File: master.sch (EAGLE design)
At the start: 24 parts, among them IC1 MEGA164P/324P/644P-PU, SW1 CI-11, U2 3V3 something

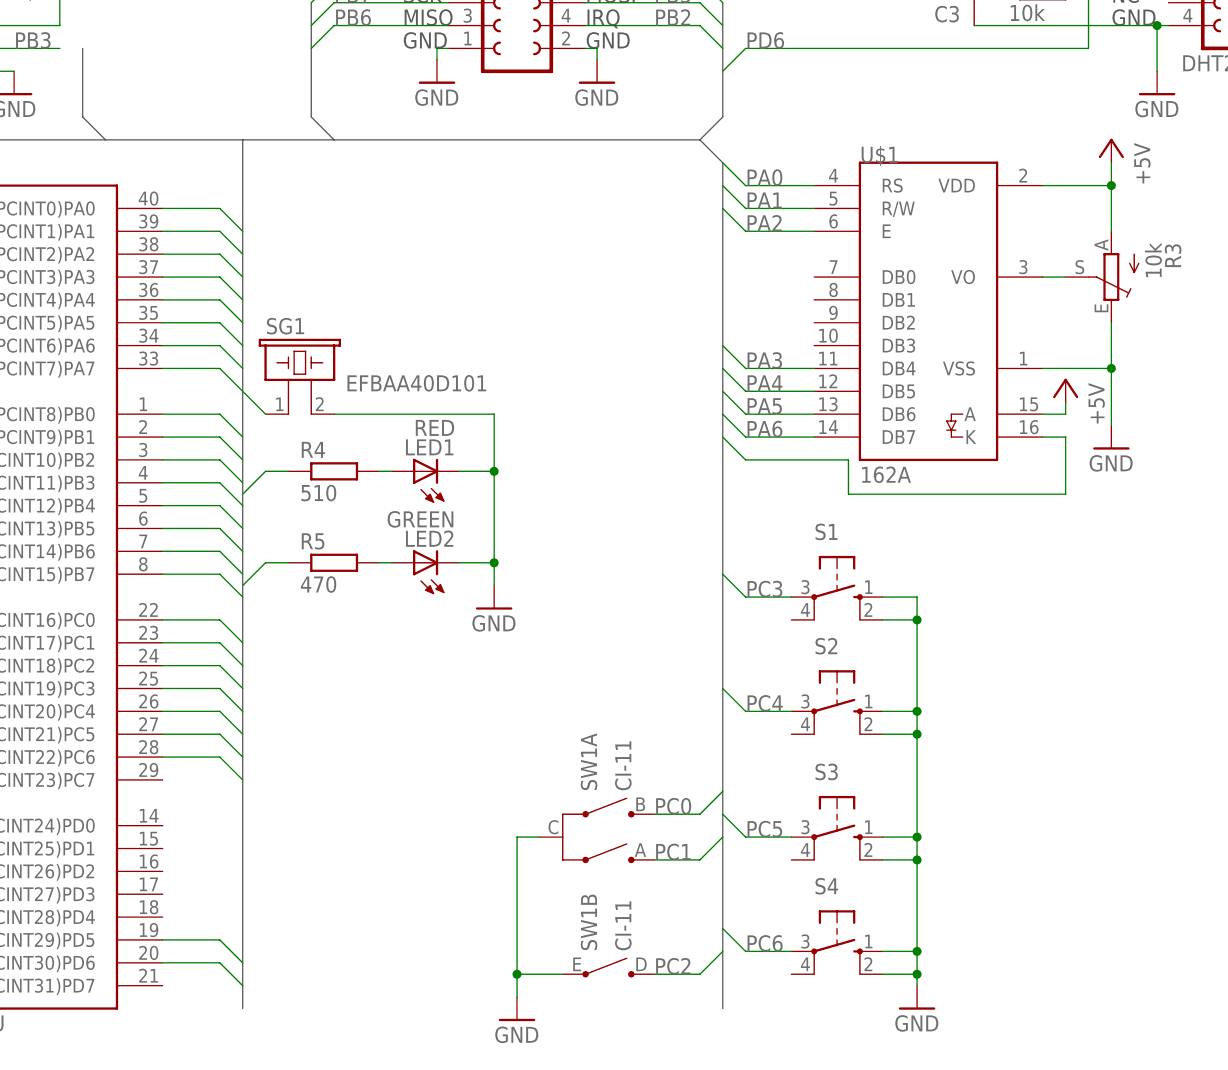
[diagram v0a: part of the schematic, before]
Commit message: added watch crystal to master, notes for sensor
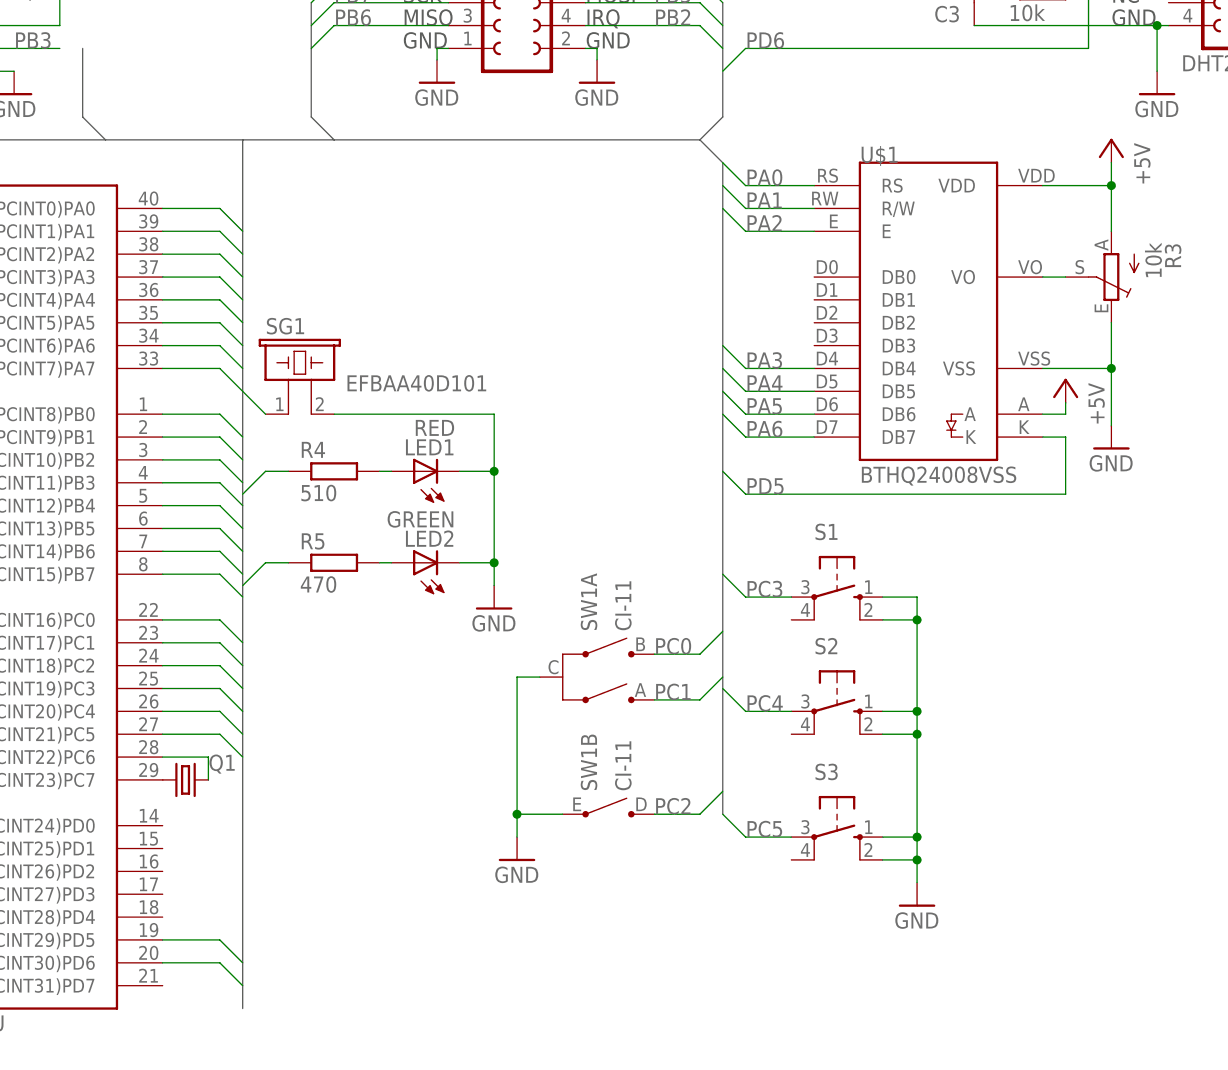
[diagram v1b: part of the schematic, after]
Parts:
- removed S4: (no value), switch-omron:10-XX
- added Q1: (no value), crystal:CRYSTALTC26H
- U$1: value 162A -> BTHQ24008VSS; device lcd_displays:162A -> lcd_displays:BTHQ24008VSS
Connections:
- removed net PC6: IC1.(TOSC1/PCINT22)PC6, S4.P
- new net N$3: IC1.(TOSC2/PCINT23)PC7, Q1.1
- new net N$4: IC1.(TOSC1/PCINT22)PC6, Q1.2
- net GND: no longer S4.S, S4.S1
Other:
- moved on the sheet: SW1A, SW1B

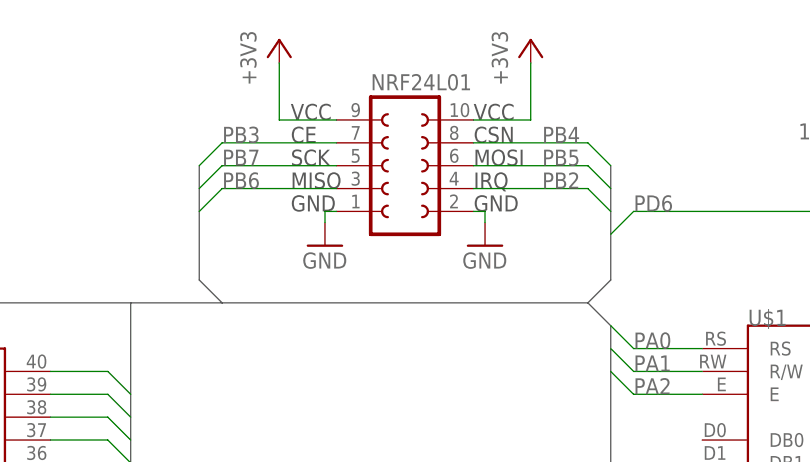
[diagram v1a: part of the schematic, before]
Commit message: series resistors for shared spi/isp interface
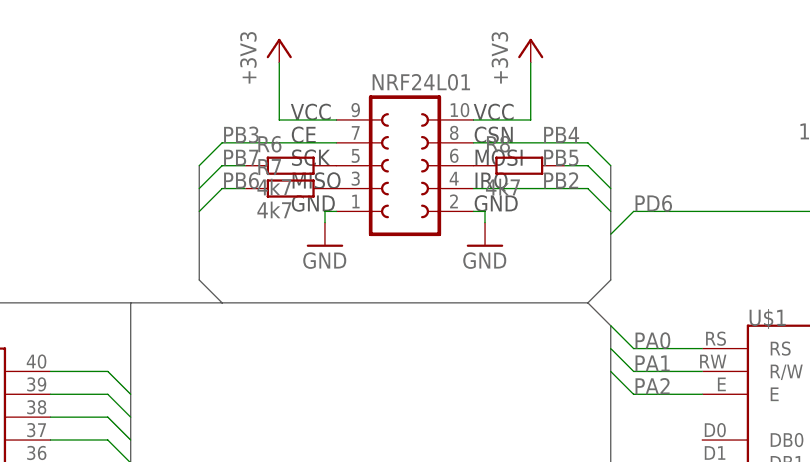
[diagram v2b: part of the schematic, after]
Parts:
- added R6, R7, R8: 4k7, rcl:R-EU_0207/7
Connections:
- new net N$5: NRF24L01.5, R6.2
- new net N$6: NRF24L01.3, R7.2
- new net N$7: NRF24L01.6, R8.1
- net PB5: now also R8.2; no longer NRF24L01.6
- net PB6: now also R7.1; no longer NRF24L01.3
- net PB7: now also R6.1; no longer NRF24L01.5
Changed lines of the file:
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@@
 <setting verticaltext="up"/>
 </settings>
-<grid distance="1.27" unitdist="mm" unit="mm" style="lines" multiple="1" display="yes" altdistance="635" altunitdist="mic" altunit="mic"/>
+<grid distance="0.1" unitdist="inch" unit="mm" style="lines" multiple="1" display="yes" altdistance="0.01" altunitdist="inch" altunit="mm"/>
 <layers>
-<layer number="1" name="Top" color="4" fill="1" visible="yes" active="no"/>
-<layer number="2" name="Route2" color="1" fill="3" visible="yes" active="no"/>
-<layer number="3" name="Route3" color="4" fill="3" visible="yes" active="no"/>
-<layer number="4" name="Route4" color="1" fill="4" visible="yes" active="no"/>
-<layer number="5" name="Route5" color="4" fill="4" visible="yes" active="no"/>
-<layer number="6" name="Route6" color="1" fill="8" visible="yes" active="no"/>
-<layer number="7" name="Route7" color="4" fill="8" visible="yes" active="no"/>
-<layer number="8" name="Route8" color="1" fill="2" visible="yes" active="no"/>
-<layer number="9" name="Route9" color="4" fill="2" visible="yes" active="no"/>
-<layer number="10" name="Route10" color="1" fill="7" visible="yes" active="no"/>
-<layer number="11" name="Route11" color="4" fill="7" visible="yes" active="no"/>
-<layer number="12" name="Route12" color="1" fill="5" visible="yes" active="no"/>
-<layer number="13" name="Route13" color="4" fill="5" visible="yes" active="no"/>
-<layer number="14" name="Route14" color="1" fill="6" visible="yes" active="no"/>
-<layer number="15" name="Route15" color="4" fill="6" visible="yes" active="no"/>
-<layer number="16" name="Bottom" color="1" fill="1" visible="yes" active="no"/>
-<layer number="17" name="Pads" color="2" fill="1" visible="yes" active="no"/>
-<layer number="18" name="Vias" color="2" fill="1" visible="yes" active="no"/>
-<layer number="19" name="Unrouted" color="6" fill="1" visible="yes" active="no"/>
-<layer number="20" name="Dimension" color="15" fill="1" visible="yes" active="no"/>
-<layer number="21" name="tPlace" color="7" fill="1" visible="yes" active="no"/>
-<layer number="22" name="bPlace" color="7" fill="1" visible="yes" active="no"/>
-<layer number="23" name="tOrigins" color="15" fill="1" visible="yes" active="no"/>
-<layer number="24" name="bOrigins" color="15" fill="1" visible="yes" active="no"/>
-<layer number="25" name="tNames" color="7" fill="1" visible="yes" active="no"/>
-<layer number="26" name="bNames" color="7" fill="1" visible="yes" active="no"/>
-<layer number="27" name="tValues" color="7" fill="1" visible="yes" active="no"/>
-<layer number="28" name="bValues" color="7" fill="1" visible="yes" active="no"/>
+<layer number="1" name="Top" color="4" fill="1" visible="no" active="no"/>
+<layer number="2" name="Route2" color="1" fill="3" visible="no" active="no"/>
+<layer number="3" name="Route3" color="4" fill="3" visible="no" active="no"/>
+<layer number="4" name="Route4" color="1" fill="4" visible="no" active="no"/>
+<layer number="5" name="Route5" color="4" fill="4" visible="no" active="no"/>
+<layer number="6" name="Route6" color="1" fill="8" visible="no" active="no"/>
+<layer number="7" name="Route7" color="4" fill="8" visible="no" active="no"/>
+<layer number="8" name="Route8" color="1" fill="2" visible="no" active="no"/>
+<layer number="9" name="Route9" color="4" fill="2" visible="no" active="no"/>
+<layer number="10" name="Route10" color="1" fill="7" visible="no" active="no"/>
+<layer number="11" name="Route11" color="4" fill="7" visible="no" active="no"/>
+<layer number="12" name="Route12" color="1" fill="5" visible="no" active="no"/>
+<layer number="13" name="Route13" color="4" fill="5" visible="no" active="no"/>
+<layer number="14" name="Route14" color="1" fill="6" visible="no" active="no"/>
+<layer number="15" name="Route15" color="4" fill="6" visible="no" active="no"/>
+<layer number="16" name="Bottom" color="1" fill="1" visible="no" active="no"/>
+<layer number="17" name="Pads" color="2" fill="1" visible="no" active="no"/>
+<layer number="18" name="Vias" color="2" fill="1" visible="no" active="no"/>
+<layer number="19" name="Unrouted" color="6" fill="1" visible="no" active="no"/>
+<layer number="20" name="Dimension" color="15" fill="1" visible="no" active="no"/>
+<layer number="21" name="tPlace" color="7" fill="1" visible="no" active="no"/>
+<layer number="22" name="bPlace" color="7" fill="1" visible="no" active="no"/>
+<layer number="23" name="tOrigins" color="15" fill="1" visible="no" active="no"/>
+<layer number="24" name="bOrigins" color="15" fill="1" visible="no" active="no"/>
+<layer number="25" name="tNames" color="7" fill="1" visible="no" active="no"/>
+<layer number="26" name="bNames" color="7" fill="1" visible="no" active="no"/>
+<layer number="27" name="tValues" color="7" fill="1" visible="no" active="no"/>
+<layer number="28" name="bValues" color="7" fill="1" visible="no" active="no"/>
 <layer number="29" name="tStop" color="7" fill="3" visible="no" active="no"/>
 <layer number="30" name="bStop" color="7" fill="6" visible="no" active="no"/>
@@
 <layer number="35" name="tGlue" color="7" fill="4" visible="no" active="no"/>
 <layer number="36" name="bGlue" color="7" fill="5" visible="no" active="no"/>
-<layer number="37" name="tTest" color="7" fill="1" visible="yes" active="no"/>
-<layer number="38" name="bTest" color="7" fill="1" visible="yes" active="no"/>
+<layer number="37" name="tTest" color="7" fill="1" visible="no" active="no"/>
+<layer number="38" name="bTest" color="7" fill="1" visible="no" active="no"/>
 <layer number="39" name="tKeepout" color="4" fill="11" visible="no" active="no"/>
 <layer number="40" name="bKeepout" color="1" fill="11" visible="no" active="no"/>
@@
 <layer number="44" name="Drills" color="7" fill="1" visible="no" active="no"/>
 <layer number="45" name="Holes" color="7" fill="1" visible="no" active="no"/>
-<layer number="46" name="Milling" color="3" fill="1" visible="yes" active="no"/>
-<layer number="47" name="Measures" color="7" fill="1" visible="yes" active="no"/>
-<layer number="48" name="Document" color="7" fill="1" visible="yes" active="no"/>
-<layer number="49" name="Reference" color="7" fill="1" visible="yes" active="no"/>
-<layer number="50" name="dxf" color="7" fill="1" visible="yes" active="no"/>
-<layer number="51" name="tDocu" color="7" fill="1" visible="yes" active="no"/>
-<layer number="52" name="bDocu" color="7" fill="1" visible="yes" active="no"/>
-<layer number="53" name="tPadExt" color="7" fill="1" visible="yes" active="no"/>
-<layer number="54" name="bPadExt" color="1" fill="1" visible="yes" active="no"/>
+<layer number="46" name="Milling" color="3" fill="1" visible="no" active="no"/>
+<layer number="47" name="Measures" color="7" fill="1" visible="no" active="no"/>
+<layer number="48" name="Document" color="7" fill="1" visible="no" active="no"/>
+<layer number="49" name="Reference" color="7" fill="1" visible="no" active="no"/>
+<layer number="50" name="dxf" color="7" fill="1" visible="no" active="no"/>
+<layer number="51" name="tDocu" color="7" fill="1" visible="no" active="no"/>
+<layer number="52" name="bDocu" color="7" fill="1" visible="no" active="no"/>
+<layer number="53" name="tPadExt" color="7" fill="1" visible="no" active="no"/>
+<layer number="54" name="bPadExt" color="1" fill="1" visible="no" active="no"/>
 <layer number="91" name="Nets" color="2" fill="1" visible="yes" active="yes"/>
 <layer number="92" name="Busses" color="1" fill="1" visible="yes" active="yes"/>
@@
 <part name="+3V3" library="supply1" deviceset="+3V3" device=""/>
 <part name="Q1" library="crystal" deviceset="CRYSTAL" device="TC26H"/>
+<part name="R6" library="rcl" deviceset="R-EU_" device="0207/7" value="4k7"/>
+<part name="R7" library="rcl" deviceset="R-EU_" device="0207/7" value="4k7"/>
+<part name="R8" library="rcl" deviceset="R-EU_" device="0207/7" value="4k7"/>
 </parts>
 <sheets>
@@
 <instance part="+3V3" gate="G$1" x="166.37" y="166.37"/>
 <instance part="Q1" gate="G$1" x="115.57" y="66.04"/>
+<instance part="R6" gate="G$1" x="139.7" y="152.4"/>
+<instance part="R7" gate="G$1" x="139.7" y="149.86"/>
+<instance part="R8" gate="G$1" x="165.1" y="152.4"/>
 </instances>
 <busses>
@@
 </segment>
 <segment>
-<pinref part="NRF24L01" gate="G$1" pin="6"/>
-<wire x1="172.72" y1="152.4" x2="160.02" y2="152.4" width="0.1524" layer="91"/>
 <label x="167.64" y="152.4" size="1.778" layer="95"/>
 <wire x1="175.26" y1="149.86" x2="172.72" y2="152.4" width="0.1524" layer="91"/>
+<pinref part="R8" gate="G$1" pin="2"/>
+<wire x1="170.18" y1="152.4" x2="172.72" y2="152.4" width="0.1524" layer="91"/>
 </segment>
 <segment>
@@
 <net name="PB7" class="0">
 <segment>
-<pinref part="NRF24L01" gate="G$1" pin="5"/>
-<wire x1="132.08" y1="152.4" x2="144.78" y2="152.4" width="0.1524" layer="91"/>
 <label x="132.08" y="152.4" size="1.778" layer="95"/>
 <wire x1="129.54" y1="149.86" x2="132.08" y2="152.4" width="0.1524" layer="91"/>
+<pinref part="R6" gate="G$1" pin="1"/>
+<wire x1="132.08" y1="152.4" x2="134.62" y2="152.4" width="0.1524" layer="91"/>
 </segment>
 <segment>
@@
 <net name="PB6" class="0">
 <segment>
-<pinref part="NRF24L01" gate="G$1" pin="3"/>
-<wire x1="144.78" y1="149.86" x2="132.08" y2="149.86" width="0.1524" layer="91"/>
 <label x="132.08" y="149.86" size="1.778" layer="95"/>
 <wire x1="129.54" y1="147.32" x2="132.08" y2="149.86" width="0.1524" layer="91"/>
+<pinref part="R7" gate="G$1" pin="1"/>
+<wire x1="132.08" y1="149.86" x2="134.62" y2="149.86" width="0.1524" layer="91"/>
 </segment>
 <segment>
@@
 </segment>
 </net>
+<net name="N$5" class="0">
+<segment>
+<pinref part="NRF24L01" gate="G$1" pin="5"/>
+<pinref part="R6" gate="G$1" pin="2"/>
+</segment>
+</net>
+<net name="N$6" class="0">
+<segment>
+<pinref part="NRF24L01" gate="G$1" pin="3"/>
+<pinref part="R7" gate="G$1" pin="2"/>
+</segment>
+</net>
+<net name="N$7" class="0">
+<segment>
+<pinref part="NRF24L01" gate="G$1" pin="6"/>
+<pinref part="R8" gate="G$1" pin="1"/>
+</segment>
+</net>

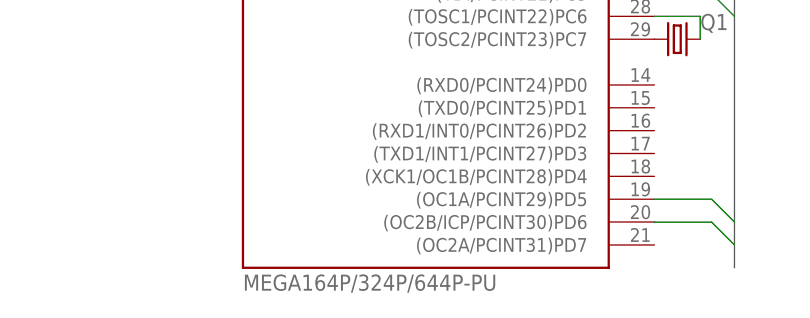
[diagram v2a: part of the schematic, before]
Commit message: atmega1284 is pin compatible
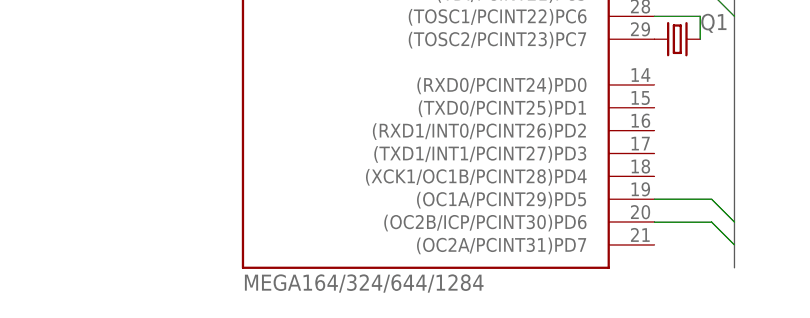
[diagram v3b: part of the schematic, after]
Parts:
- IC1: value MEGA164P/324P/644P-PU -> MEGA164/324/644/1284
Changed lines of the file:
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@@
 <setting verticaltext="up"/>
 </settings>
-<grid distance="0.1" unitdist="inch" unit="mm" style="lines" multiple="1" display="yes" altdistance="0.01" altunitdist="inch" altunit="mm"/>
+<grid distance="1.27" unitdist="mm" unit="mm" style="lines" multiple="1" display="yes" altdistance="635" altunitdist="mic" altunit="mic"/>
 <layers>
 <layer number="1" name="Top" color="4" fill="1" visible="no" active="no"/>
@@
 <part name="GND4" library="supply1" deviceset="GND" device=""/>
 <part name="U$1" library="lcd_displays" deviceset="BTHQ24008VSS" device=""/>
-<part name="IC1" library="avr-7" deviceset="MEGA164P/324P/644P-PU" device=""/>
+<part name="IC1" library="avr-7" deviceset="MEGA164P/324P/644P-PU" device="" value="MEGA164/324/644/1284"/>
 <part name="R3" library="pot" deviceset="TRIM_EU-" device="ST10" value="10k"/>
 <part name="P+7" library="supply1" deviceset="+5V" device=""/>
